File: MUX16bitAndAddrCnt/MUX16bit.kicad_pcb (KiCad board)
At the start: 2 copper layers, 149.9 x 99.1 mm, 32 parts, among them J1 Conn_01x17_Female, J2 Conn_01x17_Female, J3 Conn_01x17_Female, J4 Conn_01x17_Female, J5 Conn_01x17_Female, J6 Conn_01x01_Male, J7 Conn_01x03_Male, J8 Screw_Terminal_01x02, Q1 IRLML5203, U1 MUX4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

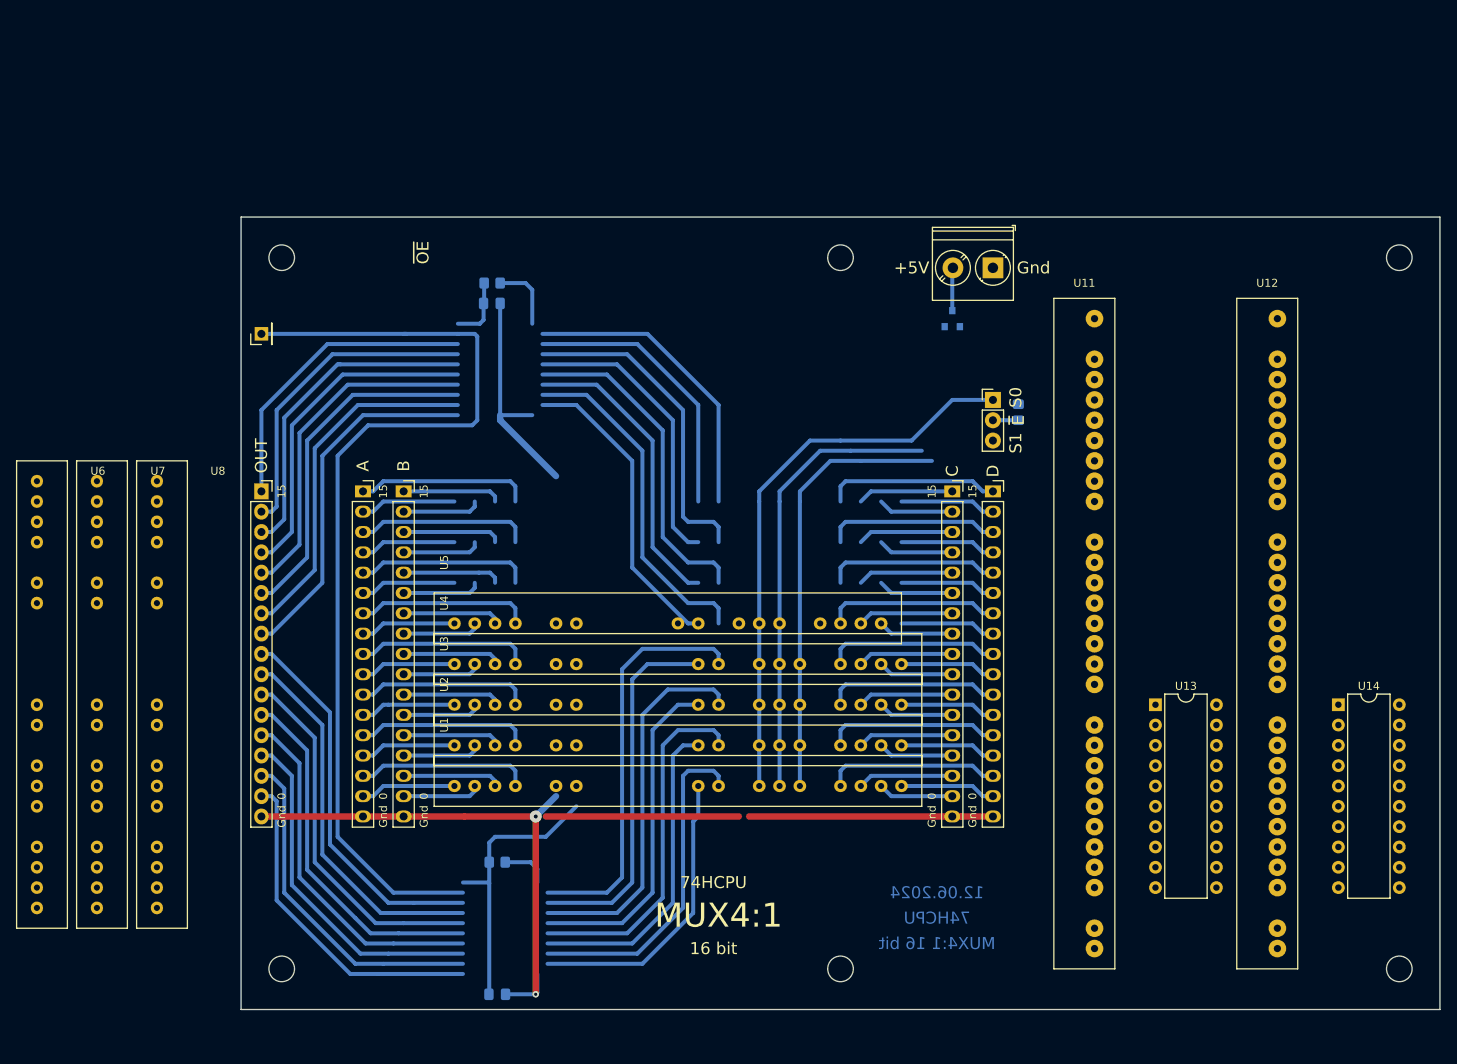
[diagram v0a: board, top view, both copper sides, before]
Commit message: Address counter in work
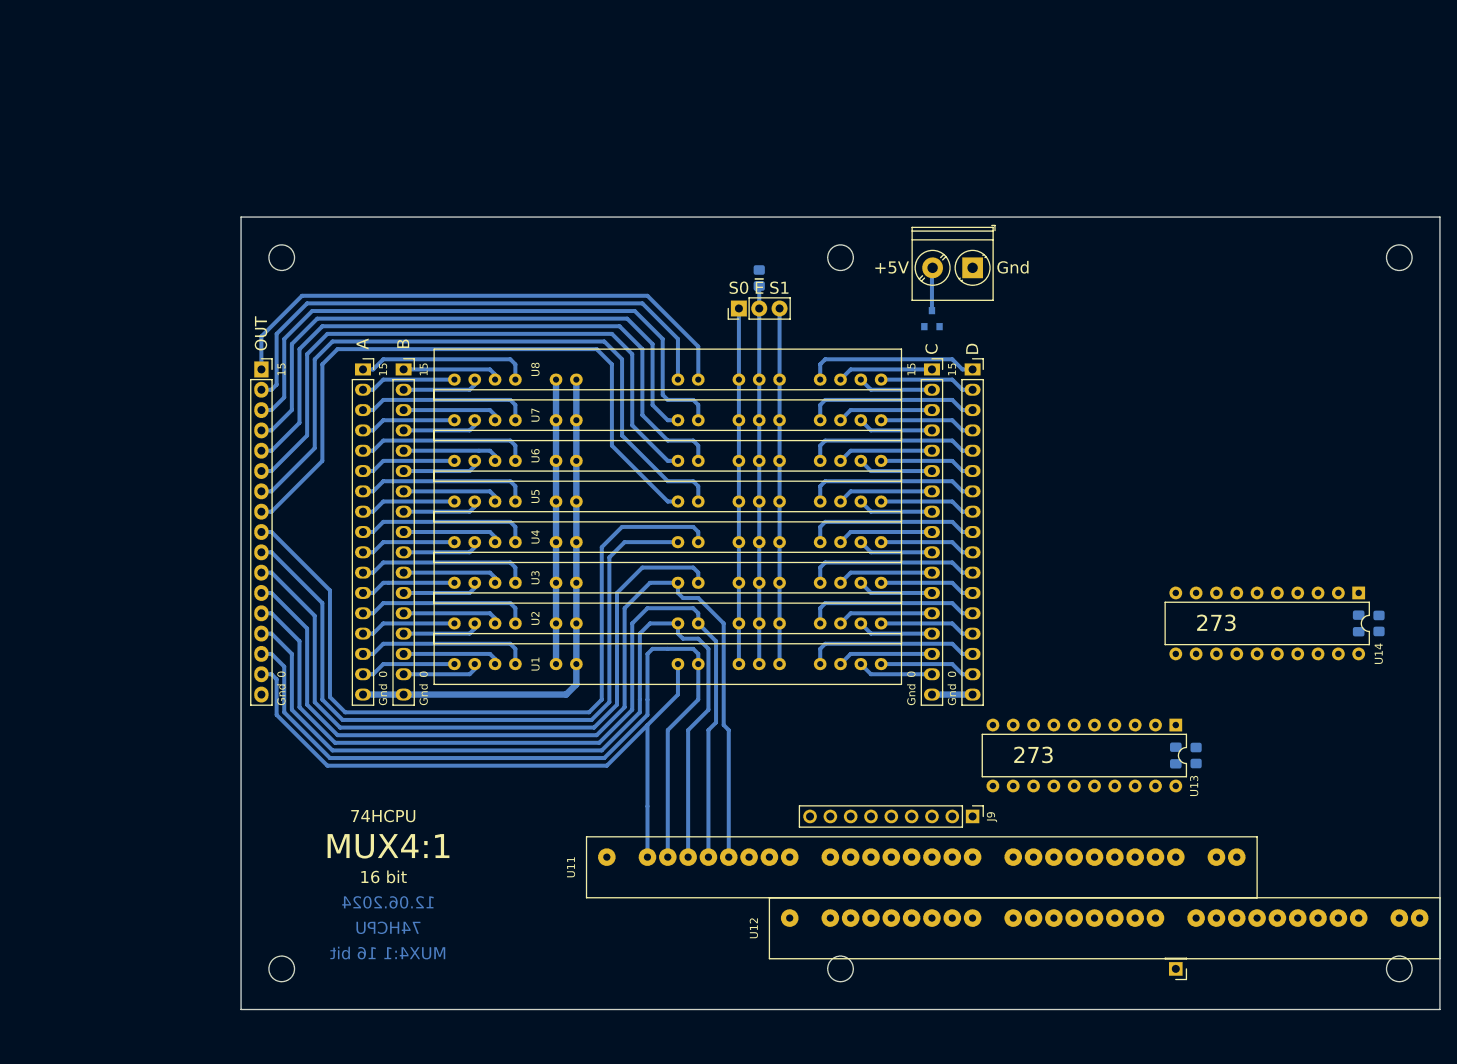
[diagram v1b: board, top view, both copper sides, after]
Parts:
- added J9: Conn_01x09_Male, Connector_PinHeader_2.54mm:PinHeader_1x09_P2.54mm_Vertical, F.Cu at (104.1, 87.6)
- moved J6 139.2 mm to (129.5, 106.7), turned to 180 degrees
- moved R2 118.7 mm to (154.9, 63.5), turned to 270 degrees
- moved C2 115.5 mm to (152.4, 63.5), turned to 90 degrees
- moved U12 96.6 mm to (81.3, 100.3), turned to 90 degrees
- moved U11 90.8 mm to (58.4, 92.7), turned to 90 degrees
- moved C1 89.9 mm to (129.5, 80.0), turned to 90 degrees
- moved R1 88.4 mm to (132.1, 80.0), turned to 270 degrees
- moved U6 52.3 mm to (39.4, 43.2), turned to 90 degrees
- moved U7 45.3 mm to (39.4, 38.1), turned to 90 degrees
- moved U8 39.3 mm to (39.4, 33.0), turned to 90 degrees
- moved R3 36.5 mm to (77.5, 20.3)
- moved J7 33.7 mm to (74.9, 24.1), turned to 90 degrees
- moved J4 15.5 mm to (104.1, 31.8)
- moved J3 15.5 mm to (99.1, 31.8)
- moved J1 15.2 mm to (27.9, 31.8)
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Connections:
- J5 pad 1: /BUS15 -> /O15
- J5 pad 10: /BUS6 -> /O6
- J5 pad 11: /BUS5 -> /O5
- J5 pad 12: /BUS4 -> /O4
- J5 pad 13: /BUS3 -> /O3
- J5 pad 14: /BUS2 -> /O2
- J5 pad 15: /BUS1 -> /O1
- J5 pad 16: /BUS0 -> /O0
- J5 pad 2: /BUS14 -> /O14
- J5 pad 3: /BUS13 -> /O13
- J5 pad 4: /BUS12 -> /O12
- J5 pad 5: /BUS11 -> /O11
- J5 pad 6: /BUS10 -> /O10
- J5 pad 7: /BUS9 -> /O9
- J5 pad 8: /BUS8 -> /O8
- J5 pad 9: /BUS7 -> /O7
- J6 pad 1: /~OE -> Net-(J6-Pad1)
- U11 pad 10: Net-(U11-Pad10) -> /CNST0
- U11 pad 11: Net-(U11-Pad11) -> /CNST1
- U11 pad 12: Net-(U11-Pad12) -> /CNST2
- U11 pad 13: Net-(U11-Pad13) -> /CNST3
- U11 pad 14: Net-(U11-Pad14) -> /CNST4
- U11 pad 15: Net-(U11-Pad15) -> /CNST5
- U11 pad 16: Net-(U11-Pad16) -> /CNST6
- U11 pad 17: Net-(U11-Pad17) -> /CNST7
- U11 pad 18: Net-(U11-Pad18) -> /N0
- U11 pad 19: Net-(U11-Pad19) -> /N1
- U11 pad 20: Net-(U11-Pad20) -> /N2
- U11 pad 21: Net-(U11-Pad21) -> /N3
- U11 pad 22: Net-(U11-Pad22) -> /N4
- U11 pad 23: Net-(U11-Pad23) -> /N5
- U11 pad 24: Net-(U11-Pad24) -> /N6
- U11 pad 25: Net-(U11-Pad25) -> /N7
- U11 pad 26: Net-(U11-Pad26) -> Net-(J6-Pad1)
- U12 pad 10: Net-(U12-Pad10) -> /CNST7
- U12 pad 11: Net-(U12-Pad11) -> /CNST7
- U12 pad 12: Net-(U12-Pad12) -> /CNST7
- U12 pad 13: Net-(U12-Pad13) -> /CNST7
- U12 pad 14: Net-(U12-Pad14) -> /CNST7
- U12 pad 15: Net-(U12-Pad15) -> /CNST7
- U12 pad 16: Net-(U12-Pad16) -> /CNST7
- U12 pad 17: Net-(U12-Pad17) -> /CNST7
- U12 pad 18: Net-(U12-Pad18) -> /N8
- U12 pad 19: Net-(U12-Pad19) -> /N9
- U12 pad 20: Net-(U12-Pad20) -> /N10
- U12 pad 21: Net-(U12-Pad21) -> /N11
- U12 pad 22: Net-(U12-Pad22) -> /N12
- U12 pad 23: Net-(U12-Pad23) -> /N13
- U12 pad 24: Net-(U12-Pad24) -> /N14
- U12 pad 25: Net-(U12-Pad25) -> /N15
- U13 pad 12: Net-(U13-Pad12) -> /D1
- U13 pad 13: Net-(U11-Pad22) -> /N1
- U13 pad 14: Net-(U11-Pad23) -> /N2
- U13 pad 15: Net-(U13-Pad15) -> /D2
- U13 pad 16: Net-(U13-Pad16) -> /D5
- U13 pad 17: Net-(U11-Pad24) -> /N5
- U13 pad 18: Net-(U11-Pad25) -> /N6
- U13 pad 19: Net-(U13-Pad19) -> /D6
- U13 pad 2: Net-(U13-Pad2) -> /D7
- U13 pad 3: Net-(U11-Pad18) -> /N7
- U13 pad 4: Net-(U11-Pad19) -> /N4
- U13 pad 5: Net-(U13-Pad5) -> /D4
- U13 pad 6: Net-(U13-Pad6) -> /D3
- U13 pad 7: Net-(U11-Pad20) -> /N3
- U13 pad 8: Net-(U11-Pad21) -> /N0
- U13 pad 9: Net-(U13-Pad9) -> /D0
- U14 pad 12: Net-(U14-Pad12) -> /D9
- U14 pad 13: Net-(U12-Pad22) -> /N9
- U14 pad 14: Net-(U12-Pad23) -> /N10
- U14 pad 15: Net-(U14-Pad15) -> /D10
- U14 pad 16: Net-(U14-Pad16) -> /D13
- U14 pad 17: Net-(U12-Pad24) -> /N13
- U14 pad 18: Net-(U12-Pad25) -> /N14
- U14 pad 19: Net-(U14-Pad19) -> /D14
- U14 pad 2: Net-(U14-Pad2) -> /D15
- U14 pad 3: Net-(U12-Pad18) -> /N15
- U14 pad 4: Net-(U12-Pad19) -> /N12
- U14 pad 5: Net-(U14-Pad5) -> /D12
- U14 pad 6: Net-(U14-Pad6) -> /D11
- U14 pad 7: Net-(U12-Pad20) -> /N11
- U14 pad 8: Net-(U12-Pad21) -> /N8
- U14 pad 9: Net-(U14-Pad9) -> /D8
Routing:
- net /~OE: track 123.4 -> 0.00 mm
- net /O8: track 0.00 -> 81.4 mm
- net GND: track 150.9 -> 70.4 mm, vias 2 -> 0
- net /O4: track 42.1 -> 118.2 mm
- net /O2: track 39.9 -> 107.5 mm
- net /O3: track 44.6 -> 111.5 mm
- net /O1: track 42.1 -> 100.7 mm
- net /BUS7: track 47.8 -> 0.00 mm
- net /BUS6: track 47.0 -> 0.00 mm
- net /O0: track 37.0 -> 83.4 mm
- net /BUS5: track 46.1 -> 0.00 mm
- net /BUS4: track 45.2 -> 0.00 mm
- net /BUS8: track 45.2 -> 0.00 mm
- net /BUS3: track 44.3 -> 0.00 mm
- net /BUS9: track 44.3 -> 0.00 mm
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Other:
- board text added: "273"
- board text removed: "245"
- board text removed: "~OE"

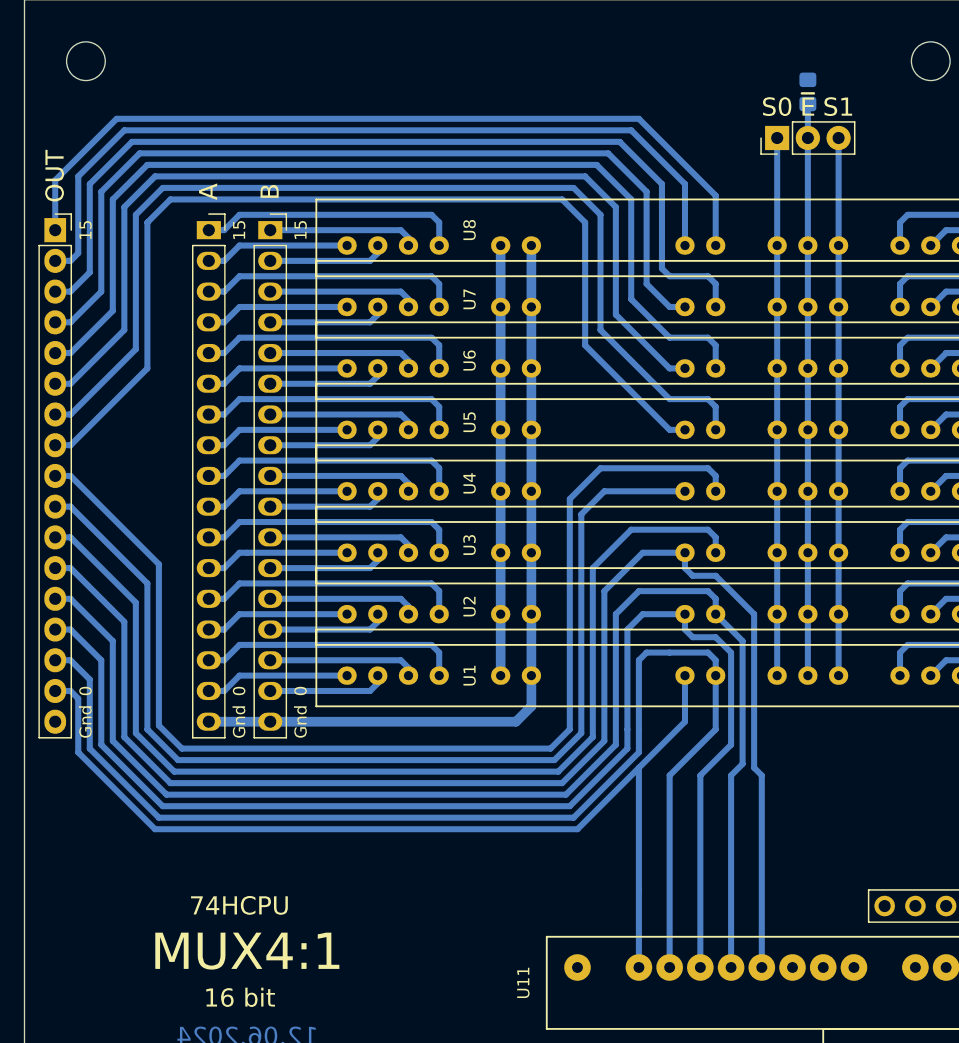
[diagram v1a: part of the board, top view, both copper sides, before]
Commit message: Address counter in work. Set power pins in center of the MUX PCB.
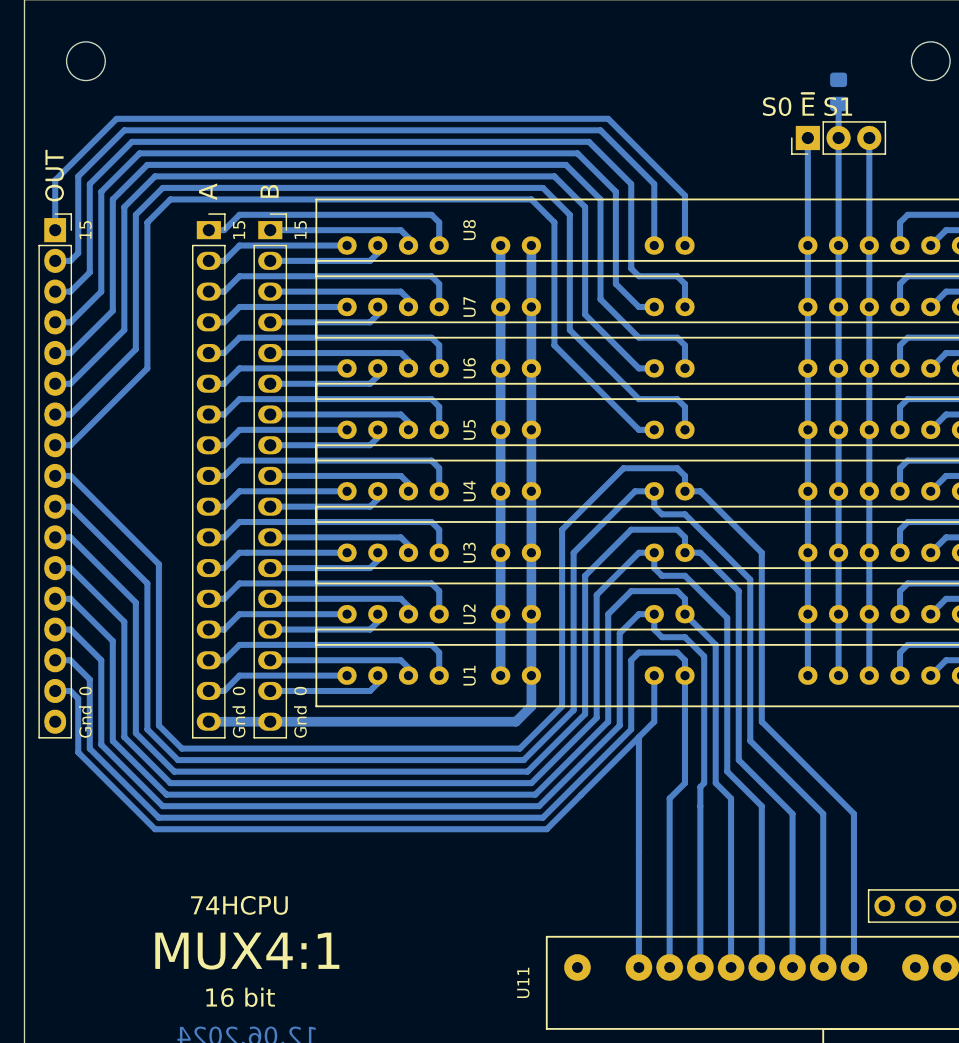
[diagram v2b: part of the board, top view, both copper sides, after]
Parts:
- moved R3 2.54 mm to (80.0, 20.3)
- moved J7 2.54 mm to (77.5, 24.1)
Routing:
- net /O6: track 87.6 -> 128.4 mm
- net /O7: track 94.1 -> 134.8 mm
- net /O5: track 87.0 -> 121.6 mm
- net /O1: track 100.7 -> 96.0 mm
- net /O2: track 107.5 -> 102.9 mm
- net /O3: track 111.5 -> 108.1 mm
- net /O4: track 118.2 -> 115.4 mm
- net /O10: track 76.9 -> 74.4 mm
- net /O8: track 81.4 -> 78.9 mm
- net /O12: track 72.4 -> 69.9 mm
- net /O11: track 79.4 -> 76.8 mm
- net /O9: track 83.9 -> 81.3 mm
- net /O15: track 67.6 -> 65.1 mm
- net /O14: track 67.2 -> 64.6 mm
- net /O13: track 74.9 -> 72.3 mm

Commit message: Address counter is almost ready ;)
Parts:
- moved R1 6.48 mm to (130.8, 73.7), turned to 0 degrees
- moved J7 3.18 mm to (77.5, 27.3)
- moved R3 3.18 mm to (80.0, 23.5)
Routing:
- net GND: track 70.4 -> 249.0 mm
- net /O14: track 64.6 -> 158.2 mm
- net /O15: track 65.1 -> 158.0 mm
- net /O12: track 69.9 -> 154.0 mm
- net /O13: track 72.3 -> 155.5 mm
- net VCC: track 35.6 -> 115.4 mm
- net /O10: track 74.4 -> 149.8 mm
- net /O11: track 76.8 -> 151.7 mm
- net /O8: track 78.9 -> 145.3 mm
- net /O9: track 81.3 -> 147.2 mm
- net /D14: track 12.0 -> 76.6 mm
- net /D13: track 21.7 -> 81.7 mm
- net /D15: track 21.7 -> 81.3 mm
- net /D10: track 12.0 -> 62.2 mm
- net /D12: track 12.0 -> 60.7 mm
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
